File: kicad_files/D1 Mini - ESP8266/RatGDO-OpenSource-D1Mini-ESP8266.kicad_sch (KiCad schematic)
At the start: 9 parts, among them J1 Screw_Terminal_01x03, J2 Screw_Terminal_01x03, J3 Screw_Terminal_01x03, Q1 2N7002, Q2 AO3400A, U1 WeMos_D1_mini

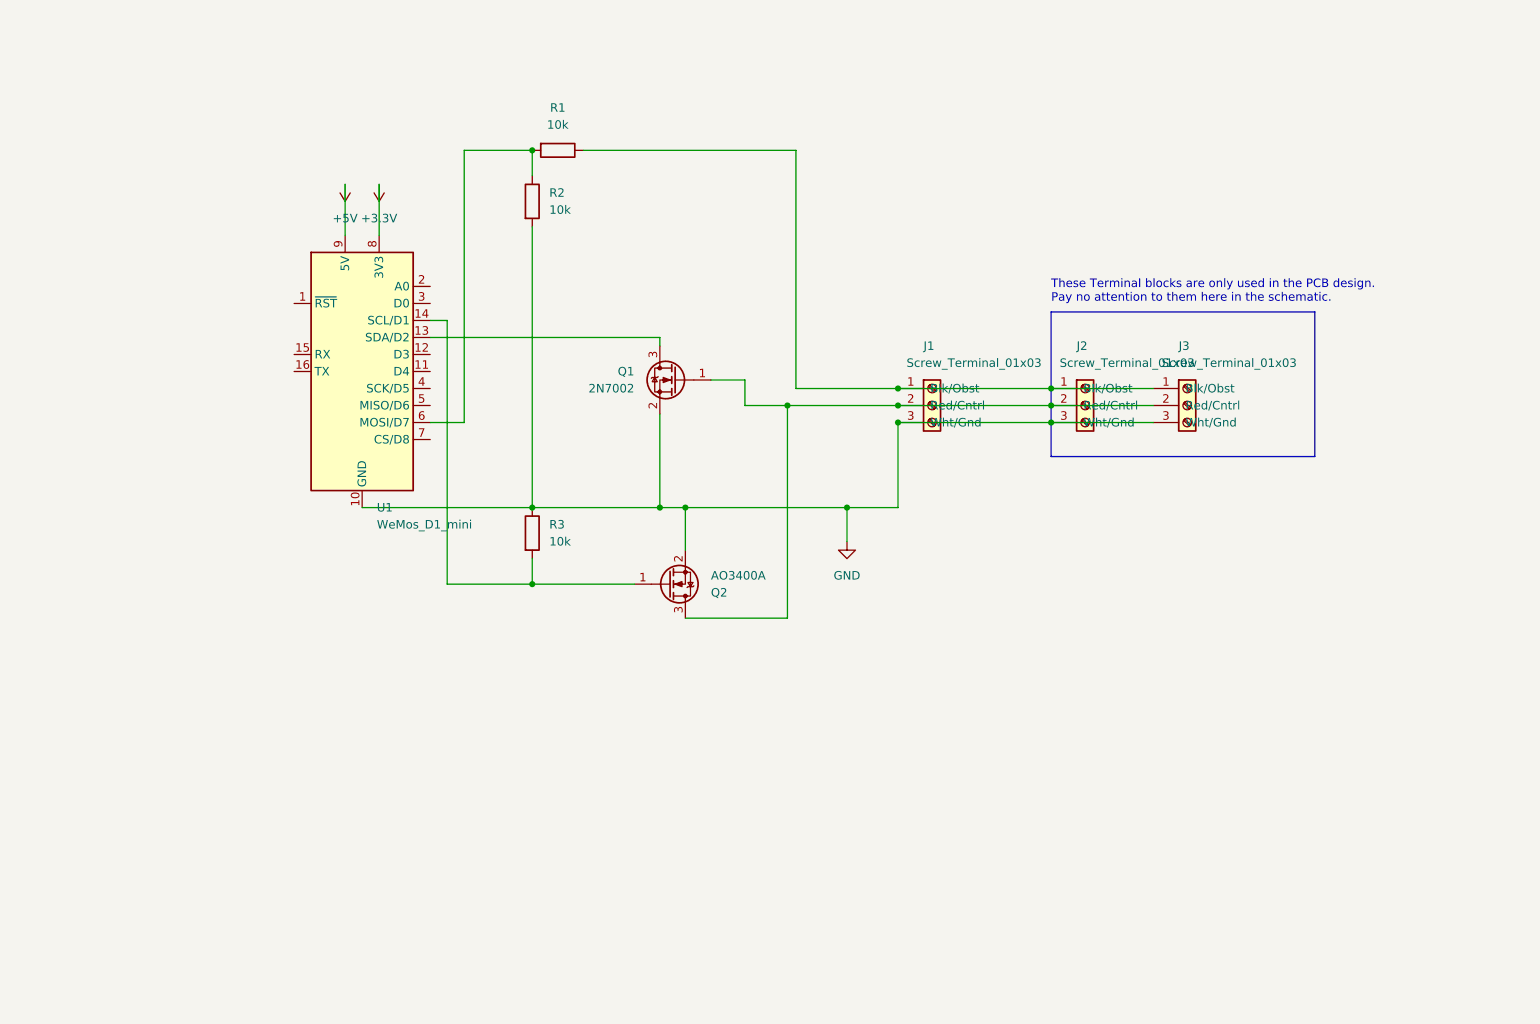
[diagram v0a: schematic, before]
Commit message: add extra output/input like original ratgdo v2.5
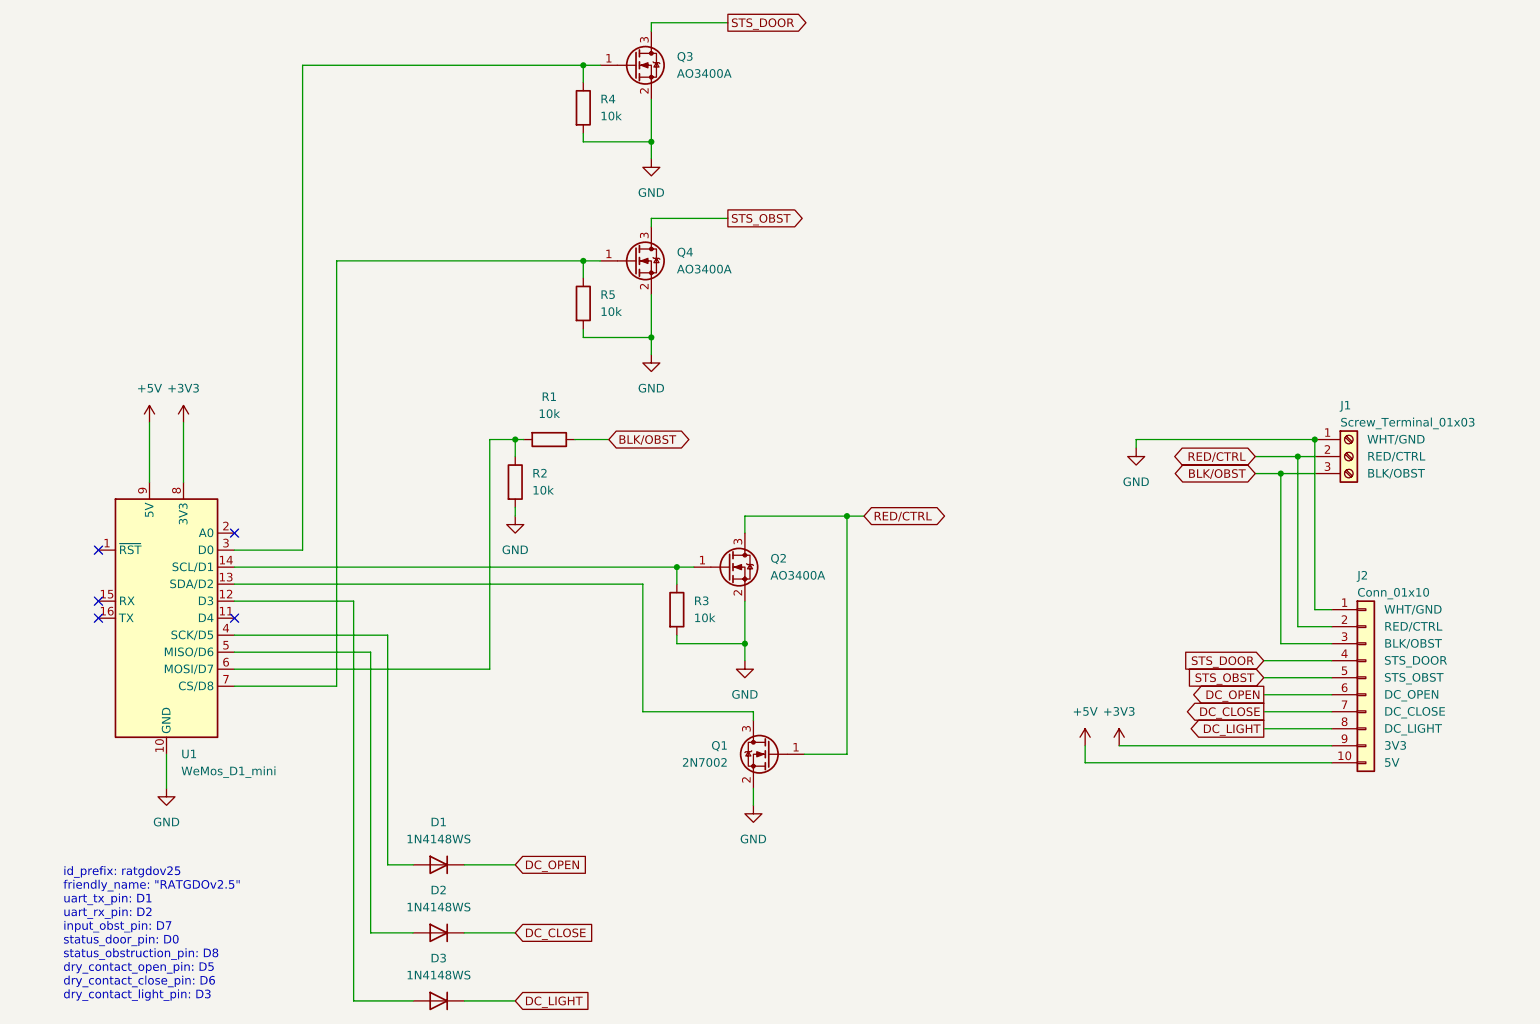
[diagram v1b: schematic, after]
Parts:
- removed J2: Screw_Terminal_01x03, Connector_Phoenix_MC:PhoenixContact_MCV_1,5_3-G-3.5_1x03_P3.50mm_Vertical, symbol Connector:Screw_Terminal_01x03
- removed J3: Screw_Terminal_01x03, Connector_PinSocket_2.54mm:PinSocket_1x03_P2.54mm_Vertical, symbol Connector:Screw_Terminal_01x03
- added D1, D2, D3: 1N4148WS, Diode_SMD:D_SOD-323_HandSoldering, symbol Diode:1N4148WS
- added J2: Conn_01x10, Connector_PinHeader_2.54mm:PinHeader_1x10_P2.54mm_Vertical, symbol Connector_Generic:Conn_01x10
- added Q3, Q4: AO3400A, Package_TO_SOT_SMD:SOT-23, symbol Transistor_FET:AO3400A
- added R4, R5: 10k, Resistor_SMD:R_0805_2012Metric, symbol Device:R
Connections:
- net +5V: now also J2.10 (5V)
- net GND: now also J1.1 (WHT/GND), R3.2, J2.1 (WHT/GND), Q3.2 (S), Q4.2 (S), R4.2, R5.2; no longer J1.3 (Wht/Gnd), R3.1
- net at Q2.1 (G), U1.14 (SCL/D1): now also R3.1; no longer R3.2
- net at U1.12 (D3): now also D3.2 (A)
- net at U1.3 (D0): now also Q3.1 (G), R4.1
- net at U1.4 (SCK/D5): now also D1.2 (A)
- net at U1.5 (MISO/D6): now also D2.2 (A)
- net at U1.7 (CS/D8): now also Q4.1 (G), R5.1
- net BLK/OBST: now reaches R1.1
- net BLK/OBST: now also J1.3 (BLK/OBST), J2.3 (BLK/OBST); no longer J1.1 (Blk/Obst)
- net RED/CTRL: now reaches J1.2 (RED/CTRL), Q1.1 (G), Q2.3 (D)
- net RED/CTRL: now also J2.2 (RED/CTRL)
- net +3.3V renamed +3V3
- net +3V3: now also J2.9 (3V3)
- new net DC_CLOSE: D2.1 (K), J2.7 (DC_CLOSE)
- new net DC_LIGHT: D3.1 (K), J2.8 (DC_LIGHT)
- new net DC_OPEN: D1.1 (K), J2.6 (DC_OPEN)
- new net STS_DOOR: J2.4 (STS_DOOR), Q3.3 (D)
- new net STS_OBST: J2.5 (STS_OBST), Q4.3 (D)
- no-connect marks 0 -> 5
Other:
- note added: "id_prefix: ratgdov25 friendly_name: "RATGDOv2.5" uart_tx_pin: D1 uart_rx_pin: D2 input_obst_pin: D7 status_door_pin: D0 status_obstruction_pin: D8 dry_contact_open_pin: D5 dry_contact_close_pin: D6 dry_contact_light_pin: D3"
- note removed: "These Terminal blocks are only used in the PCB design. Pay no attention to them here in the schematic."
- moved on the sheet: J1, Q1, Q2, R1, R2, R3, U1

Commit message: laid out pcba with new outline and keepout
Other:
- company: (none) -> T Fox
- title: (none) -> RAT-RATGDO TUBEX ESP8266
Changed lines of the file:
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@@
 (kicad_sch (version 20230121) (generator eeschema)
-  (paper "A4")
+  (paper "USLetter")
+  (title_block
+    (title "RAT-RATGDO TUBEX ESP8266")
+    (date "2023-11-02")
+    (rev "2.5.0")
+    (company "T Fox")
+  )
   (junction (at 152.4 106.68) (diameter 0) (color 0 0 0 0)
   )

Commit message: relayout of board
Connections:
- net ESP_TX: now reaches Q2.1 (G), R3.1, U1.14 (SCL/D1)
- net ESP_RX: now reaches Q1.3 (D), U1.13 (SDA/D2)
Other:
- moved on the sheet: D1, D2, D3, J1, Q1, Q2, Q3, Q4, R1, R2, R3, R4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

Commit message: dual connector
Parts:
- added J3: Screw_Terminal_01x02, TerminalBlock_Phoenix:TerminalBlock_Phoenix_MKDS-1,5-2_1x02_P5.00mm_Horizontal, symbol Connector:Screw_Terminal_01x02
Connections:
- net +3V3: now also J3.1 (3V3)
- net +5V: now also J3.2 (5V)
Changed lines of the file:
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@@
   (junction (at 119.38 53.34) (diameter 0) (color 0 0 0 0)
+  )
+  (junction (at 222.25 140.97) (diameter 0) (color 0 0 0 0)
+  )
+  (junction (at 219.71 143.51) (diameter 0) (color 0 0 0 0)
   )
   (no_connect (at 34.29 91.44))
@@
     (stroke (width 0) (type default))
   )
+  (wire (pts (xy 224.79 154.94) (xy 222.25 154.94))
+    (stroke (width 0) (type default))
+  )
   (wire (pts (xy 214.63 138.43) (xy 224.79 138.43))
     (stroke (width 0) (type default))
@@
     (stroke (width 0) (type default))
   )
+  (wire (pts (xy 224.79 157.48) (xy 219.71 157.48))
+    (stroke (width 0) (type default))
+  )
   (wire (pts (xy 224.79 123.19) (xy 219.71 123.19))
     (stroke (width 0) (type default))
@@
     (stroke (width 0) (type default))
   )
+  (wire (pts (xy 222.25 140.97) (xy 224.79 140.97))
+    (stroke (width 0) (type default))
+  )
   (wire (pts (xy 73.66 80.01) (xy 83.82 80.01))
     (stroke (width 0) (type default))
@@
     (stroke (width 0) (type default))
   )
-  (wire (pts (xy 224.79 143.51) (xy 187.96 143.51))
+  (wire (pts (xy 219.71 157.48) (xy 219.71 143.51))
+    (stroke (width 0) (type default))
+  )
+  (wire (pts (xy 224.79 143.51) (xy 219.71 143.51))
     (stroke (width 0) (type default))
   )
@@
     (stroke (width 0) (type default))
   )
-  (wire (pts (xy 193.04 140.97) (xy 224.79 140.97))
+  (wire (pts (xy 193.04 140.97) (xy 222.25 140.97))
     (stroke (width 0) (type default))
   )
@@
     (stroke (width 0) (type default))
   )
+  (wire (pts (xy 219.71 143.51) (xy 187.96 143.51))
+    (stroke (width 0) (type default))
+  )
   (wire (pts (xy 222.25 95.25) (xy 222.25 120.65))
     (stroke (width 0) (type default))
@@
   )
   (wire (pts (xy 54.61 91.44) (xy 59.69 91.44))
+    (stroke (width 0) (type default))
+  )
+  (wire (pts (xy 222.25 154.94) (xy 222.25 140.97))
     (stroke (width 0) (type default))
   )
@@
         )
       )
+    )
+  )
+  (symbol (lib_id "Connector:Screw_Terminal_01x02") (at 229.87 154.94 0) (unit 1)
+    (in_bom yes) (on_board yes) (dnp no)
+    (property "Reference" "J3" (at 228.6 149.86 0)
+      (effects (font (size 1.27 1.27)) (justify left))
+    )
+    (property "Value" "Screw_Terminal_01x02" (at 228.6 152.4 0)
+      (effects (font (size 1.27 1.27)) (justify left))
+    )
+    (property "Footprint" "TerminalBlock_Phoenix:TerminalBlock_Phoenix_MKDS-1,5-2_1x02_P5.00mm_Horizontal" (at 229.87 154.94 0)
+      (effects (font (size 1.27 1.27)) hide)
+    )
+    (property "Datasheet" "~" (at 229.87 154.94 0)
+      (effects (font (size 1.27 1.27)) hide)
+    )
+    (pin "1")
+    (pin "2")
+    (instances
+      (project "RatGDO-OpenSource-D1Mini-ESP8266"
+        (path "/d526daf5-1a87-4c4a-b8db-6120ccadc008"
+          (reference "J3") (unit 1)
+        )
+      )

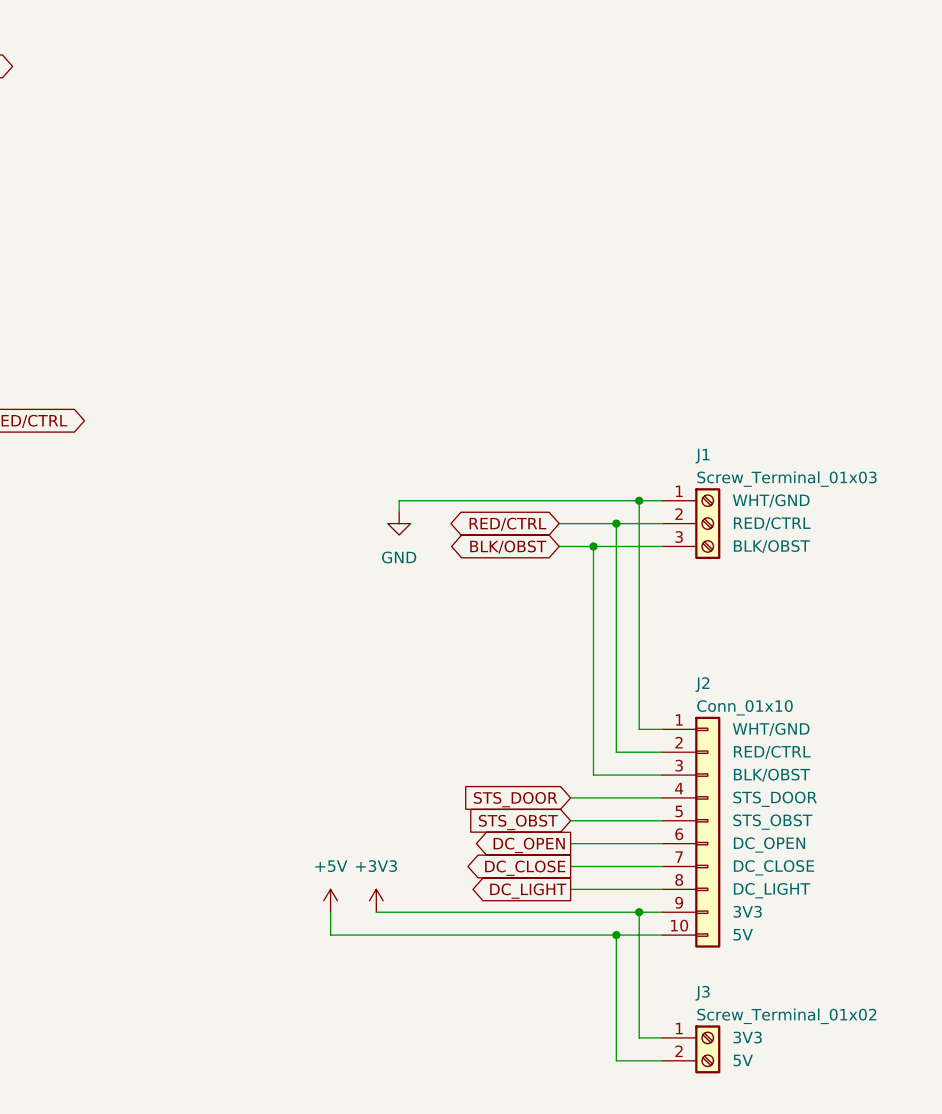
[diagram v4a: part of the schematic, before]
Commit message: Addition of 12V DC DC supply
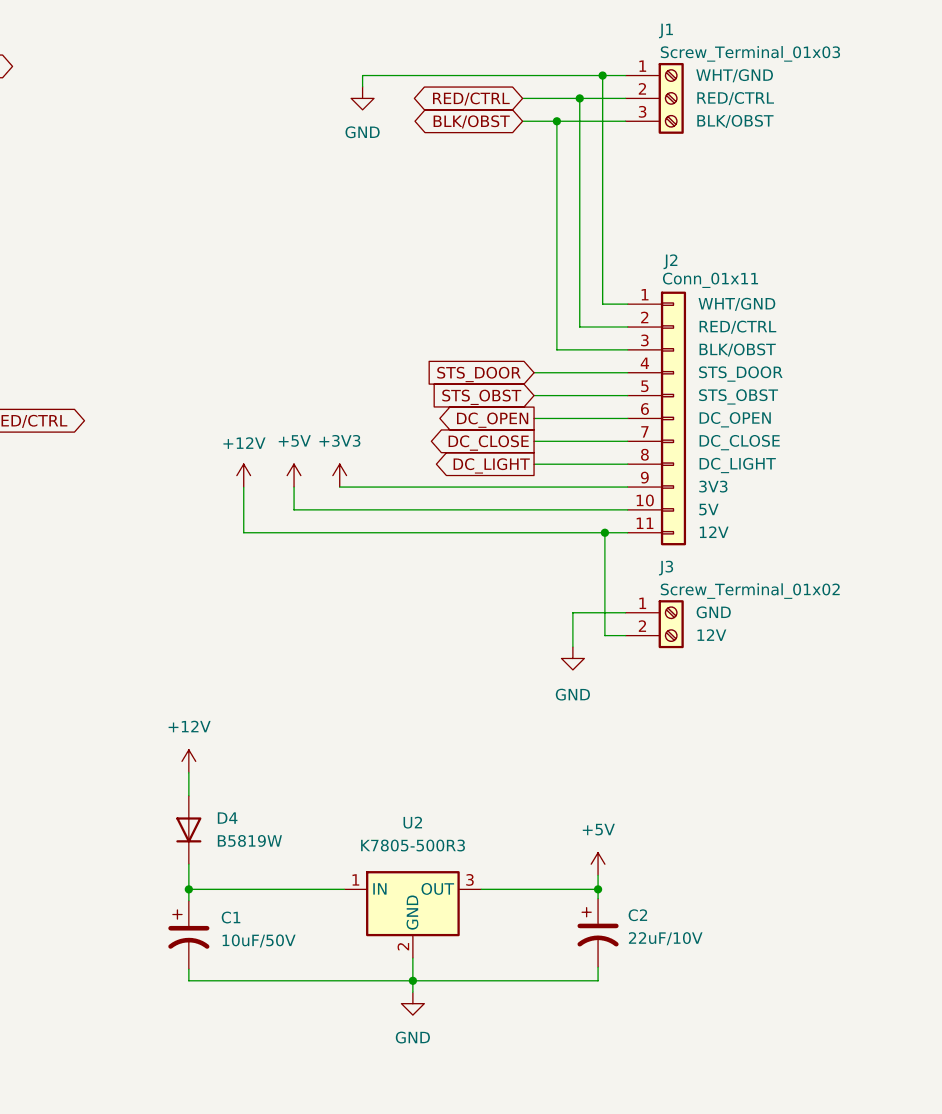
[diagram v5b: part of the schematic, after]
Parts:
- added C1: 10uF/50V, Capacitor_SMD:C_0805_2012Metric_Pad1.18x1.45mm_HandSolder, symbol Device:C_Polarized_US
- added C2: 22uF/10V, Capacitor_SMD:C_0805_2012Metric_Pad1.18x1.45mm_HandSolder, symbol Device:C_Polarized_US
- added D4: B5819W, Diode_SMD:D_SOD-123, symbol Diode:1N4448WS
- added U2: K7805-500R3, Converter_DCDC:Converter_DCDC_RECOM_R-78HB-0.5_THT, symbol Converter_DCDC:OKI-78SR-5_1.5-W36-C
- J2: value Conn_01x10 -> Conn_01x11; footprint Connector_PinHeader_2.54mm:PinHeader_1x10_P2.54mm_Vertical -> Connector_PinHeader_2.54mm:PinHeader_1x11_P2.54mm_Vertical; symbol Connector_Generic:Conn_01x10 -> Connector_Generic:Conn_01x11
- Q1, Q2, Q3, Q4: footprint Package_TO_SOT_SMD:SOT-23 -> Package_TO_SOT_SMD:SOT-23_Handsoldering
- R1, R2, R3, R4, R5: footprint Resistor_SMD:R_0805_2012Metric -> Resistor_SMD:R_0805_2012Metric_Pad1.20x1.40mm_HandSolder
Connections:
- net +3V3: no longer J3.1 (3V3)
- net +5V: now also C2.1, U2.3 (OUT); no longer J3.2 (5V)
- net GND: now also J3.1 (GND), C1.2, C2.2, U2.2 (GND)
- new net: C1.1, D4.1 (K), U2.1 (IN)
- new net +12V: D4.2 (A), J2.11 (12V), J3.2 (12V)
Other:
- moved on the sheet: J1, J3

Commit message: rename
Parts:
- removed C1: 10uF/50V, Capacitor_SMD:C_0805_2012Metric_Pad1.18x1.45mm_HandSolder, symbol Device:C_Polarized_US
- removed C2: 22uF/10V, Capacitor_SMD:C_0805_2012Metric_Pad1.18x1.45mm_HandSolder, symbol Device:C_Polarized_US
- removed D1, D2, D3: 1N4148WS, Diode_SMD:D_SOD-323_HandSoldering, symbol Diode:1N4148WS
- removed D4: B5819W, Diode_SMD:D_SOD-123, symbol Diode:1N4448WS
- removed J2: Conn_01x11, Connector_PinHeader_2.54mm:PinHeader_1x11_P2.54mm_Vertical, symbol Connector_Generic:Conn_01x11
- removed J3: Screw_Terminal_01x02, TerminalBlock_Phoenix:TerminalBlock_Phoenix_MKDS-1,5-2_1x02_P5.00mm_Horizontal, symbol Connector:Screw_Terminal_01x02
- removed Q3, Q4: AO3400A, Package_TO_SOT_SMD:SOT-23_Handsoldering, symbol Transistor_FET:AO3400A
- removed R4, R5: 10k, Resistor_SMD:R_0805_2012Metric_Pad1.20x1.40mm_HandSolder, symbol Device:R
- removed U2: K7805-500R3, Converter_DCDC:Converter_DCDC_RECOM_R-78HB-0.5_THT, symbol Converter_DCDC:OKI-78SR-5_1.5-W36-C
- added J2: Screw_Terminal_01x03, Connector_Phoenix_MC:PhoenixContact_MCV_1,5_3-G-3.5_1x03_P3.50mm_Vertical, symbol Connector:Screw_Terminal_01x03
- added J3: Screw_Terminal_01x03, Connector_PinSocket_2.54mm:PinSocket_1x03_P2.54mm_Vertical, symbol Connector:Screw_Terminal_01x03
- Q1, Q2: footprint Package_TO_SOT_SMD:SOT-23_Handsoldering -> Package_TO_SOT_SMD:SOT-23
- R1, R2, R3: footprint Resistor_SMD:R_0805_2012Metric_Pad1.20x1.40mm_HandSolder -> Resistor_SMD:R_0805_2012Metric
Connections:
- net GND: now also J1.3 (Wht/Gnd), R3.1, J2.3 (Wht/Gnd), J3.3 (Wht/Gnd); no longer J1.1 (WHT/GND), R3.2
- net +3V3 renamed +3.3V
- net BLK/OBST: no longer names the net of R1.1
- net BLK/OBST: now also J1.1 (Blk/Obst), J2.1 (Blk/Obst), J3.1 (Blk/Obst); no longer J1.3 (BLK/OBST)
- net ESP_RX: no longer names the net of Q1.3 (D), U1.13 (SDA/D2)
- net ESP_TX: no longer names the net of Q2.1 (G), U1.14 (SCL/D1)
- net ESP_TX: now also R3.2; no longer R3.1
- net RED/CTRL: no longer names the net of J1.2 (Red/Cntrl), Q1.1 (G), Q2.3 (D)
- net RED/CTRL: now also J2.2 (Red/Cntrl), J3.2 (Red/Cntrl)
- no-connect marks 5 -> 0
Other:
- note added: "These Terminal blocks are only used in the PCB design. Pay no attention to them here in the schematic."
- note removed: "id_prefix: ratgdov25 friendly_name: "RATGDOv2.5" uart_tx_pin: D1 uart_rx_pin: D2 input_obst_pin: D7 status_door_pin: D0 status_obstruction_pin: D8 dry_contact_open_pin: D5 dry_contact_close_pin: D6 dry_contact_light_pin: D3"
- company: T Fox -> (none)
- title: RAT-RATGDO TUBEX ESP8266 -> (none)
- moved on the sheet: J1, Q1, Q2, R1, R2, R3, U1
